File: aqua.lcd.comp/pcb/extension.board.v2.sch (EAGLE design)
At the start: 60 parts, among them IC1 NCP1117ST50T3G, T1 IRFR024NPBF, T10 BC847BSMD, T11 IRFR024NPBF, T12 BC847BSMD, T13 BC847BSMD, T2 BC847BSMD, T3 IRFR024NPBF, T4 BC847BSMD, T5 IRFR024NPBF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

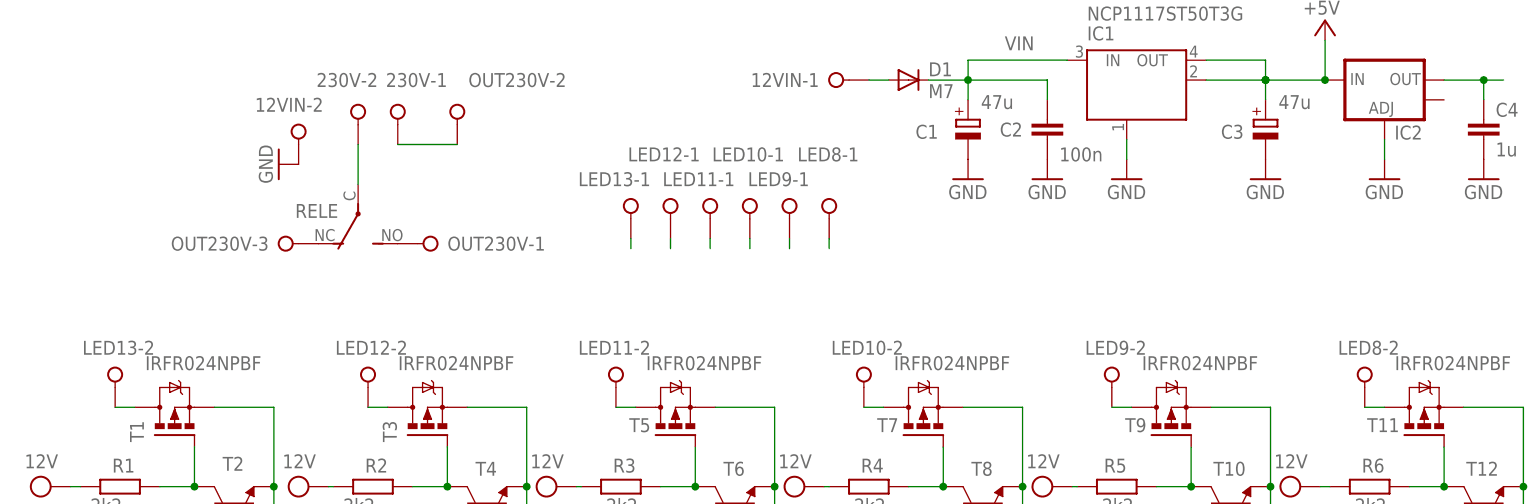
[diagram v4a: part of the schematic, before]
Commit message: modified for makefile https://github.com/sudar/Arduino-Makefile
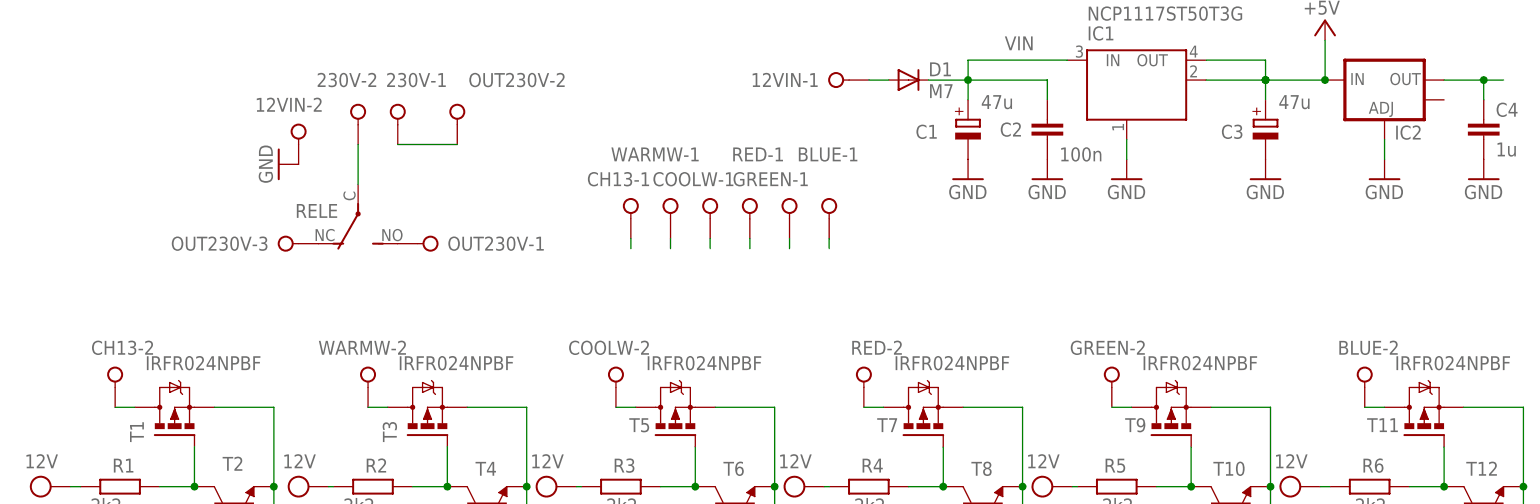
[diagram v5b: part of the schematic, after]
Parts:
- renumbered LED10 to RED, LED11 to COOLW, LED12 to WARMW, LED13 to CH13, LED8 to BLUE, LED9 to GREEN
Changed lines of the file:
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@@
 </classes>
 <parts>
-<part name="LED8" library="con-wago-508" deviceset="W237-02P" device=""/>
-<part name="LED9" library="con-wago-508" deviceset="W237-02P" device=""/>
-<part name="LED10" library="con-wago-508" deviceset="W237-02P" device=""/>
-<part name="LED11" library="con-wago-508" deviceset="W237-02P" device=""/>
-<part name="LED12" library="con-wago-508" deviceset="W237-02P" device=""/>
-<part name="LED13" library="con-wago-508" deviceset="W237-02P" device=""/>
+<part name="BLUE" library="con-wago-508" deviceset="W237-02P" device=""/>
+<part name="GREEN" library="con-wago-508" deviceset="W237-02P" device=""/>
+<part name="RED" library="con-wago-508" deviceset="W237-02P" device=""/>
+<part name="COOLW" library="con-wago-508" deviceset="W237-02P" device=""/>
+<part name="WARMW" library="con-wago-508" deviceset="W237-02P" device=""/>
+<part name="CH13" library="con-wago-508" deviceset="W237-02P" device=""/>
 <part name="12VIN" library="con-wago-508" deviceset="W237-02P" device=""/>
 <part name="SERIAL" library="pinhead" deviceset="PINHD-1X6" device=""/>
@@
 </plain>
 <instances>
-<instance part="LED8" gate="-1" x="116.84" y="104.14" smashed="yes" rot="R270">
+<instance part="BLUE" gate="-1" x="116.84" y="104.14" smashed="yes" rot="R270">
 <attribute name="NAME" x="120.65" y="110.744" size="1.778" layer="95" rot="R180"/>
 </instance>
-<instance part="LED8" gate="-2" x="185.42" y="82.55" smashed="yes" rot="R270">
+<instance part="BLUE" gate="-2" x="185.42" y="82.55" smashed="yes" rot="R270">
 <attribute name="VALUE" x="187.96" y="82.55" size="1.778" layer="96" rot="R270"/>
 <attribute name="NAME" x="189.865" y="85.979" size="1.778" layer="95" rot="R180"/>
 </instance>
-<instance part="LED9" gate="-1" x="111.76" y="104.14" smashed="yes" rot="R270">
+<instance part="GREEN" gate="-1" x="111.76" y="104.14" smashed="yes" rot="R270">
 <attribute name="NAME" x="114.3" y="107.569" size="1.778" layer="95" rot="R180"/>
 </instance>
-<instance part="LED9" gate="-2" x="153.035" y="82.55" smashed="yes" rot="R270">
+<instance part="GREEN" gate="-2" x="153.035" y="82.55" smashed="yes" rot="R270">
 <attribute name="VALUE" x="155.575" y="82.55" size="1.778" layer="96" rot="R270"/>
 <attribute name="NAME" x="157.48" y="85.979" size="1.778" layer="95" rot="R180"/>
 </instance>
-<instance part="LED10" gate="-1" x="106.68" y="104.14" smashed="yes" rot="R270">
+<instance part="RED" gate="-1" x="106.68" y="104.14" smashed="yes" rot="R270">
 <attribute name="NAME" x="111.125" y="110.744" size="1.778" layer="95" rot="R180"/>
 </instance>
-<instance part="LED10" gate="-2" x="121.285" y="82.55" smashed="yes" rot="R270">
+<instance part="RED" gate="-2" x="121.285" y="82.55" smashed="yes" rot="R270">
 <attribute name="VALUE" x="123.825" y="82.55" size="1.778" layer="96" rot="R270"/>
 <attribute name="NAME" x="126.365" y="85.979" size="1.778" layer="95" rot="R180"/>
 </instance>
-<instance part="LED11" gate="-1" x="101.6" y="104.14" smashed="yes" rot="R270">
+<instance part="COOLW" gate="-1" x="101.6" y="104.14" smashed="yes" rot="R270">
 <attribute name="NAME" x="104.775" y="107.569" size="1.778" layer="95" rot="R180"/>
 </instance>
-<instance part="LED11" gate="-2" x="89.535" y="82.55" smashed="yes" rot="R270">
+<instance part="COOLW" gate="-2" x="89.535" y="82.55" smashed="yes" rot="R270">
 <attribute name="VALUE" x="92.075" y="82.55" size="1.778" layer="96" rot="R270"/>
 <attribute name="NAME" x="93.98" y="85.979" size="1.778" layer="95" rot="R180"/>
 </instance>
-<instance part="LED12" gate="-1" x="96.52" y="104.14" smashed="yes" rot="R270">
+<instance part="WARMW" gate="-1" x="96.52" y="104.14" smashed="yes" rot="R270">
 <attribute name="NAME" x="100.33" y="110.744" size="1.778" layer="95" rot="R180"/>
 </instance>
-<instance part="LED12" gate="-2" x="57.785" y="82.55" smashed="yes" rot="R270">
+<instance part="WARMW" gate="-2" x="57.785" y="82.55" smashed="yes" rot="R270">
 <attribute name="VALUE" x="60.325" y="82.55" size="1.778" layer="96" rot="R270"/>
 <attribute name="NAME" x="62.865" y="85.979" size="1.778" layer="95" rot="R180"/>
 </instance>
-<instance part="LED13" gate="-1" x="91.44" y="104.14" smashed="yes" rot="R270">
+<instance part="CH13" gate="-1" x="91.44" y="104.14" smashed="yes" rot="R270">
 <attribute name="NAME" x="93.98" y="107.569" size="1.778" layer="95" rot="R180"/>
 </instance>
-<instance part="LED13" gate="-2" x="25.4" y="82.55" smashed="yes" rot="R270">
+<instance part="CH13" gate="-2" x="25.4" y="82.55" smashed="yes" rot="R270">
 <attribute name="VALUE" x="27.94" y="82.55" size="1.778" layer="96" rot="R270"/>
 <attribute name="NAME" x="30.48" y="85.979" size="1.778" layer="95" rot="R180"/>
@@
 <net name="N$13" class="0">
 <segment>
-<pinref part="LED13" gate="-2" pin="KL"/>
+<pinref part="CH13" gate="-2" pin="KL"/>
 <wire x1="27.94" y1="77.47" x2="25.4" y2="77.47" width="0.1524" layer="91"/>
 <pinref part="T1" gate="G$1" pin="D"/>
@@
 <wire x1="60.325" y1="77.47" x2="57.785" y2="77.47" width="0.1524" layer="91"/>
 <pinref part="T3" gate="G$1" pin="D"/>
-<pinref part="LED12" gate="-2" pin="KL"/>
+<pinref part="WARMW" gate="-2" pin="KL"/>
 </segment>
 </net>
@@
 <wire x1="92.075" y1="77.47" x2="89.535" y2="77.47" width="0.1524" layer="91"/>
 <pinref part="T5" gate="G$1" pin="D"/>
-<pinref part="LED11" gate="-2" pin="KL"/>
+<pinref part="COOLW" gate="-2" pin="KL"/>
 </segment>
 </net>
@@
 <wire x1="123.825" y1="77.47" x2="121.285" y2="77.47" width="0.1524" layer="91"/>
 <pinref part="T7" gate="G$1" pin="D"/>
-<pinref part="LED10" gate="-2" pin="KL"/>
+<pinref part="RED" gate="-2" pin="KL"/>
 </segment>
 </net>
@@
 <wire x1="155.575" y1="77.47" x2="153.035" y2="77.47" width="0.1524" layer="91"/>
 <pinref part="T9" gate="G$1" pin="D"/>
-<pinref part="LED9" gate="-2" pin="KL"/>
+<pinref part="GREEN" gate="-2" pin="KL"/>
 </segment>
 </net>
@@
 <wire x1="187.96" y1="77.47" x2="185.42" y2="77.47" width="0.1524" layer="91"/>
 <pinref part="T11" gate="G$1" pin="D"/>
-<pinref part="LED8" gate="-2" pin="KL"/>
+<pinref part="BLUE" gate="-2" pin="KL"/>
 </segment>
 </net>
@@
 </segment>
 <segment>
-<pinref part="LED8" gate="-1" pin="KL"/>
+<pinref part="BLUE" gate="-1" pin="KL"/>
 <wire x1="116.84" y1="99.06" x2="116.84" y2="97.79" width="0.1524" layer="91"/>
 </segment>
 <segment>
-<pinref part="LED9" gate="-1" pin="KL"/>
+<pinref part="GREEN" gate="-1" pin="KL"/>
 <wire x1="111.76" y1="99.06" x2="111.76" y2="97.79" width="0.1524" layer="91"/>
 </segment>
 <segment>
-<pinref part="LED10" gate="-1" pin="KL"/>
+<pinref part="RED" gate="-1" pin="KL"/>
 <wire x1="106.68" y1="99.06" x2="106.68" y2="97.79" width="0.1524" layer="91"/>
 </segment>
 <segment>
-<pinref part="LED11" gate="-1" pin="KL"/>
+<pinref part="COOLW" gate="-1" pin="KL"/>
 <wire x1="101.6" y1="99.06" x2="101.6" y2="97.79" width="0.1524" layer="91"/>
 </segment>
 <segment>
-<pinref part="LED12" gate="-1" pin="KL"/>
+<pinref part="WARMW" gate="-1" pin="KL"/>
 <wire x1="96.52" y1="99.06" x2="96.52" y2="97.79" width="0.1524" layer="91"/>
 </segment>
 <segment>
-<pinref part="LED13" gate="-1" pin="KL"/>
+<pinref part="CH13" gate="-1" pin="KL"/>
 <wire x1="91.44" y1="99.06" x2="91.44" y2="97.79" width="0.1524" layer="91"/>
 </segment>

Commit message: first
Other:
- moved on the sheet: D2, R13, RELE, T13
